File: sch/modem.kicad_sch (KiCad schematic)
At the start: 0 parts

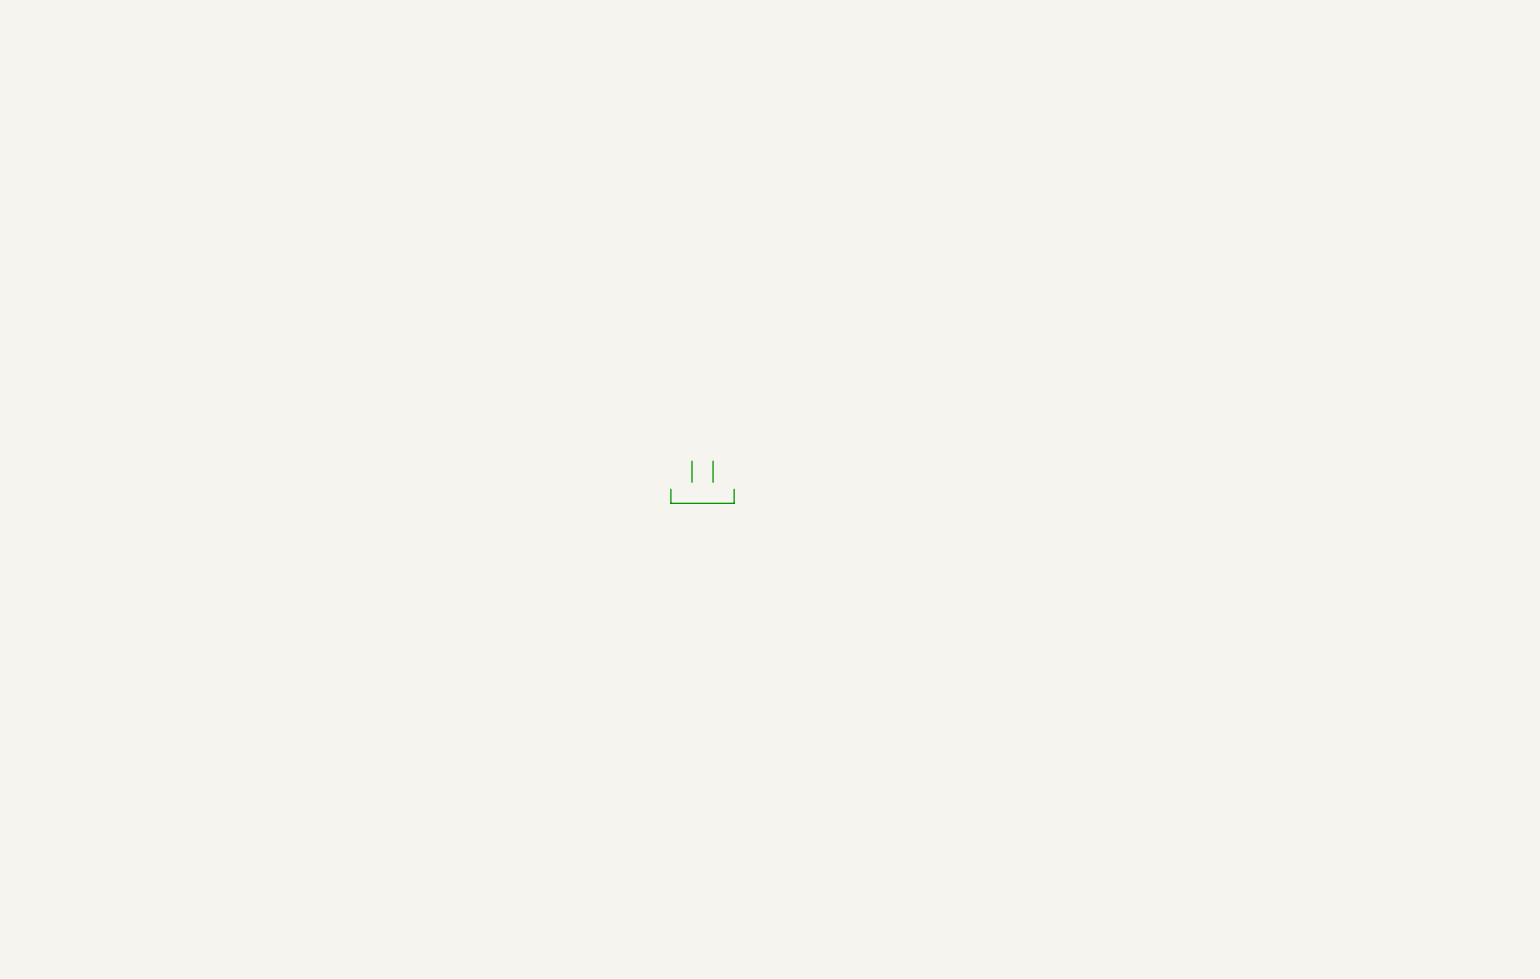
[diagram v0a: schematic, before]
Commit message: Put in Rc7620, not complete
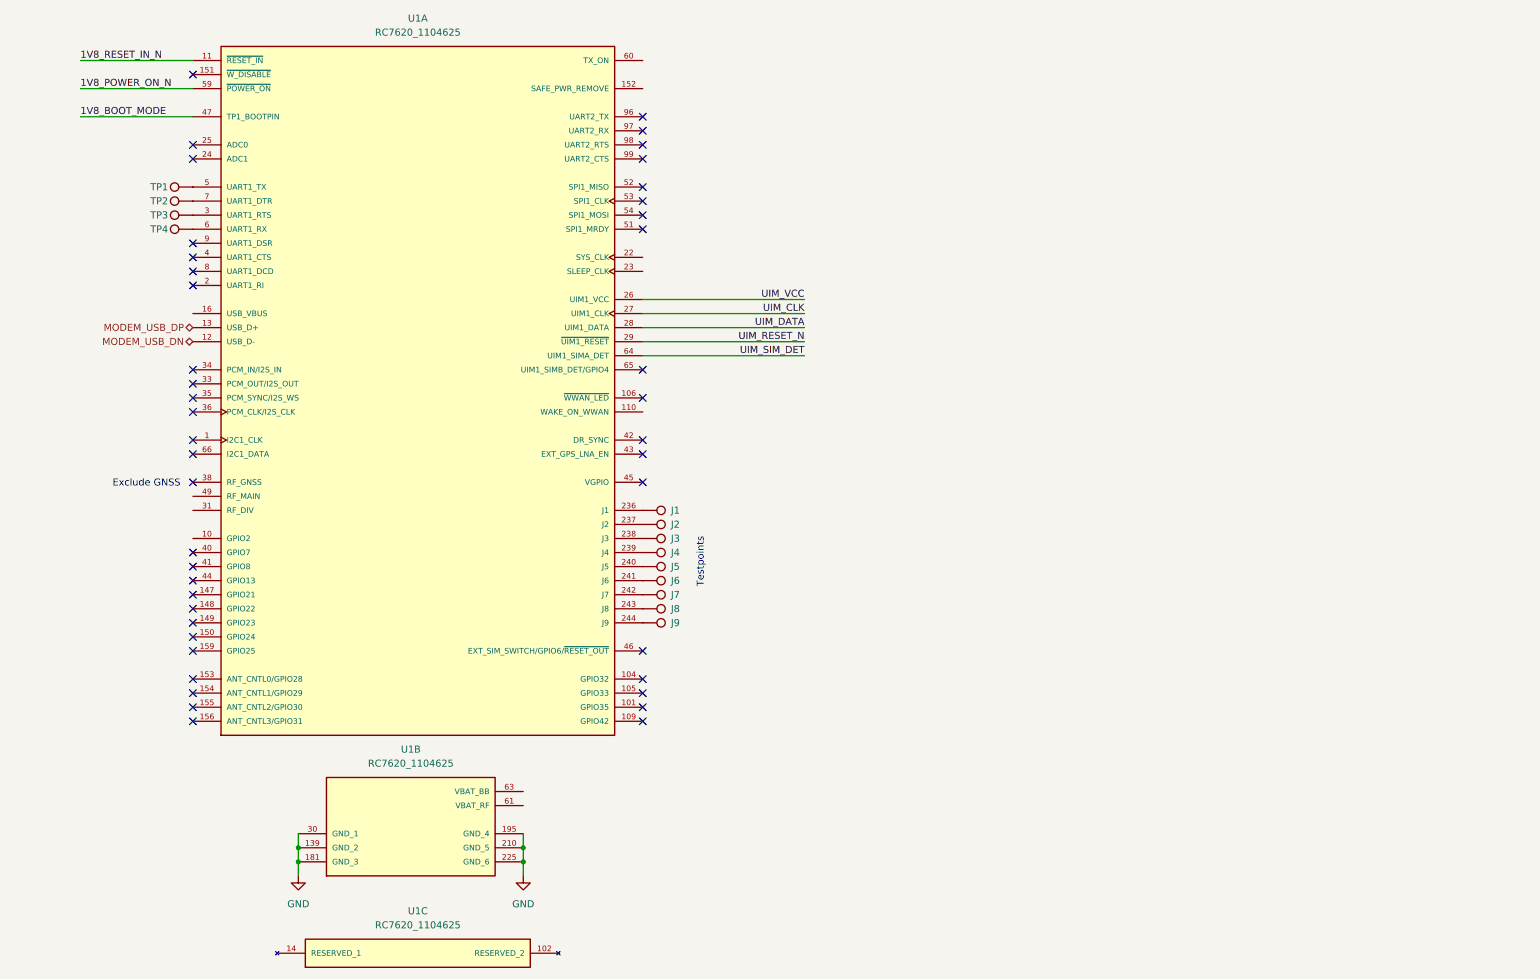
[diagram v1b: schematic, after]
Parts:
- added J1, J2, J3, J4, J5, J6, J7, J8, J9: TestPoint, symbol Connector:TestPoint
- added TP1, TP2, TP3, TP4: T1, symbol Connector:TestPoint
- added U1: RC7620_1104625, RC7620_1104625:XCVR_RC7620_1104625, symbol RC7620_1104625:RC7620_1104625
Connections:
- new net: TP2.1, U1.7 (UART1_DTR)
- new net: TP3.1, U1.3 (UART1_RTS)
- new net: J8.1, U1.243 (J8)
- new net: J7.1, U1.242 (J7)
- new net: J1.1, U1.236 (J1)
- new net: J2.1, U1.237 (J2)
- new net: J3.1, U1.238 (J3)
- new net: J4.1, U1.239 (J4)
- new net: J5.1, U1.240 (J5)
- new net: J6.1, U1.241 (J6)
- new net: J9.1, U1.244 (J9)
- new net: TP1.1, U1.5 (UART1_TX)
- new net: TP4.1, U1.6 (UART1_RX)
- new net: U1.100 (RESERVED_1), U1.14 (RESERVED_1), U1.15 (RESERVED_1), U1.17 (RESERVED_1), U1.18 (RESERVED_1), U1.19 (RESERVED_1), U1.20 (RESERVED_1), U1.21 (RESERVED_1), U1.55 (RESERVED_1), U1.56 (RESERVED_1), U1.57 (RESERVED_1), U1.58 (RESERVED_1), U1.71 (RESERVED_1), U1.72 (RESERVED_1), U1.73 (RESERVED_1), U1.74 (RESERVED_1), U1.75 (RESERVED_1), U1.76 (RESERVED_1), U1.77 (RESERVED_1), U1.78 (RESERVED_1), U1.79 (RESERVED_1), U1.80 (RESERVED_1), U1.81 (RESERVED_1), U1.82 (RESERVED_1), U1.83 (RESERVED_1), U1.84 (RESERVED_1), U1.85 (RESERVED_1), U1.86 (RESERVED_1), U1.87 (RESERVED_1), U1.88 (RESERVED_1), U1.89 (RESERVED_1), U1.90 (RESERVED_1), U1.91 (RESERVED_1), U1.92 (RESERVED_1), U1.93 (RESERVED_1), U1.94 (RESERVED_1), U1.95 (RESERVED_1)
- new net: U1.102 (RESERVED_2), U1.103 (RESERVED_2), U1.107 (RESERVED_2), U1.108 (RESERVED_2), U1.114 (RESERVED_2), U1.115 (RESERVED_2), U1.116 (RESERVED_2), U1.117 (RESERVED_2), U1.118 (RESERVED_2), U1.119 (RESERVED_2), U1.120 (RESERVED_2), U1.121 (RESERVED_2), U1.122 (RESERVED_2), U1.123 (RESERVED_2), U1.124 (RESERVED_2), U1.129 (RESERVED_2), U1.130 (RESERVED_2), U1.131 (RESERVED_2), U1.132 (RESERVED_2), U1.133 (RESERVED_2), U1.134 (RESERVED_2), U1.135 (RESERVED_2), U1.140 (RESERVED_2), U1.141 (RESERVED_2), U1.142 (RESERVED_2), U1.143 (RESERVED_2), U1.144 (RESERVED_2), U1.145 (RESERVED_2), U1.146 (RESERVED_2), U1.160 (RESERVED_2), U1.161 (RESERVED_2), U1.162 (RESERVED_2), U1.163 (RESERVED_2), U1.164 (RESERVED_2), U1.165 (RESERVED_2), U1.166 (RESERVED_2)
- new net 1V8_BOOT_MODE: U1.47 (TP1_BOOTPIN)
- new net 1V8_POWER_ON_N: U1.59 (~{POWER_ON})
- new net 1V8_RESET_IN_N: U1.11 (~{RESET_IN})
- new net GND: U1.111 (GND_1), U1.113 (GND_1), U1.125 (GND_1), U1.128 (GND_1), U1.136 (GND_1), U1.139 (GND_2), U1.167 (GND_2), U1.168 (GND_2), U1.169 (GND_2), U1.170 (GND_2), U1.171 (GND_2), U1.172 (GND_2), U1.173 (GND_2), U1.174 (GND_2), U1.175 (GND_2), U1.176 (GND_2), U1.177 (GND_2), U1.178 (GND_2), U1.179 (GND_2), U1.180 (GND_2), U1.181 (GND_3), U1.182 (GND_3), U1.183 (GND_3), U1.184 (GND_3), U1.185 (GND_3), U1.186 (GND_3), U1.187 (GND_3), U1.188 (GND_3), U1.189 (GND_3), U1.190 (GND_3), U1.191 (GND_3), U1.192 (GND_3), U1.193 (GND_3), U1.194 (GND_3), U1.195 (GND_4), U1.196 (GND_4), U1.197 (GND_4), U1.198 (GND_4), U1.199 (GND_4), U1.200 (GND_4), U1.201 (GND_4), U1.202 (GND_4), U1.203 (GND_4), U1.204 (GND_4), U1.205 (GND_4), U1.206 (GND_4), U1.207 (GND_4), U1.208 (GND_4), U1.209 (GND_4), U1.210 (GND_5), U1.211 (GND_5), U1.212 (GND_5), U1.213 (GND_5), U1.214 (GND_5), U1.215 (GND_5), U1.216 (GND_5), U1.217 (GND_5), U1.218 (GND_5), U1.219 (GND_5), U1.220 (GND_5), U1.221 (GND_5), U1.222 (GND_5), U1.223 (GND_5), U1.224 (GND_5), U1.225 (GND_6), U1.226 (GND_6), U1.227 (GND_6), U1.228 (GND_6), U1.229 (GND_6), U1.230 (GND_6), U1.231 (GND_6), U1.232 (GND_6), U1.233 (GND_6), U1.234 (GND_6), U1.30 (GND_1), U1.32 (GND_1), U1.37 (GND_1), U1.39 (GND_1), U1.48 (GND_1), U1.50 (GND_1), U1.67 (GND_1), U1.68 (GND_1), U1.69 (GND_1), U1.70 (GND_1)
- new net MODEM_USB_DN: U1.12 (USB_D-)
- new net MODEM_USB_DP: U1.13 (USB_D+)
- new net UIM_CLK: U1.27 (UIM1_CLK)
- new net UIM_DATA: U1.28 (UIM1_DATA)
- new net UIM_RESET_N: U1.29 (~{UIM1_RESET})
- new net UIM_SIM_DET: U1.64 (UIM1_SIMA_DET)
- new net UIM_VCC: U1.26 (UIM1_VCC)
- new net VBAT_BB: U1.158 (VBAT_BB), U1.63 (VBAT_BB)
- new net VBAT_RF: U1.157 (VBAT_RF), U1.61 (VBAT_RF), U1.62 (VBAT_RF)
- no-connect marks 0 -> 44
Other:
- note added: "Exclude GNSS"
- note added: "Testpoints"

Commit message: Added powersupply and simcard, still missing 4 ESD diodes to simcard
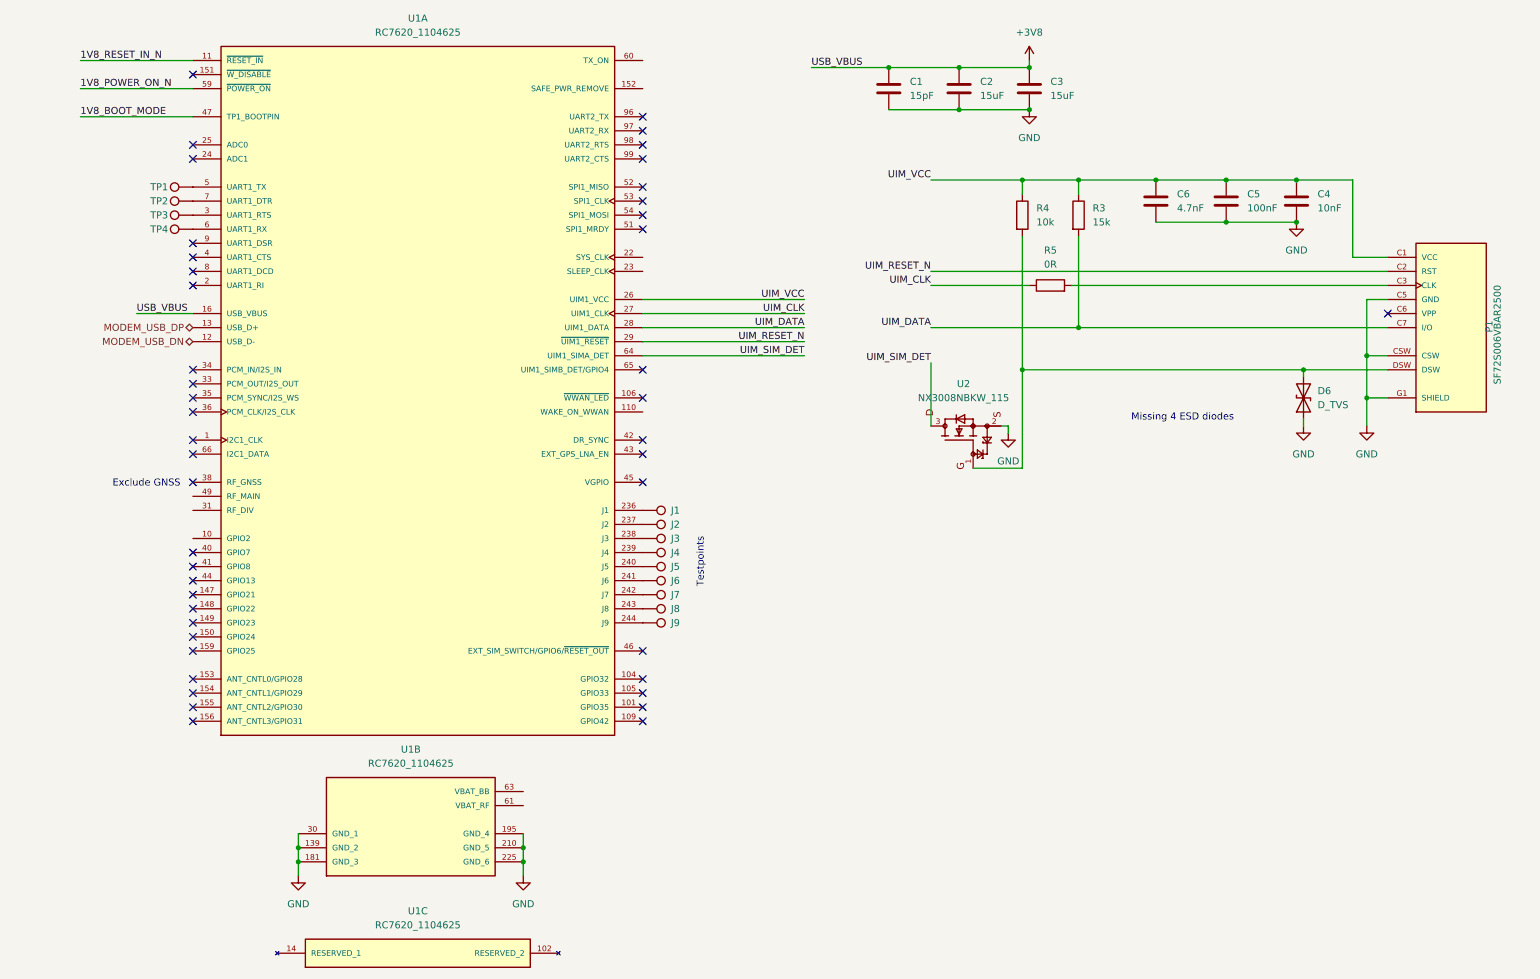
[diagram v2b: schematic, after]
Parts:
- added C1: 15pF, symbol Device:C
- added C2, C3: 15uF, symbol Device:C
- added C4: 10nF, symbol Device:C
- added C5: 100nF, symbol Device:C
- added C6: 4.7nF, symbol Device:C
- added D6: D_TVS, symbol Device:D_TVS
- added P1: SF72S006VBAR2500, SF72S006VBAR2500:JAE_SF72S006VBAR2500, symbol SF72S006VBAR2500:SF72S006VBAR2500
- added R3: 15k, symbol Device:R
- added R4: 10k, symbol Device:R
- added R5: 0R, symbol Device:R
- added U2: NX3008NBKW_115, NX3008NBKW_115:SOT65P210X110-3N, symbol NX3008NBKW_115:NX3008NBKW_115
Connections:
- net GND: now also C1.2, C2.2, C3.2, C4.2, C5.2, C6.2, D6.1 (A1), P1.C5 (GND), P1.CSW, P1.G1 (SHIELD), P1.G10 (SHIELD), P1.G2 (SHIELD), P1.G3 (SHIELD), P1.G4 (SHIELD), P1.G5 (SHIELD), P1.G6 (SHIELD), P1.G7 (SHIELD), P1.G8 (SHIELD), P1.G9 (SHIELD), U2.2
- net UIM_CLK: now also R5.1
- net UIM_DATA: now also P1.C7 (I/O), R3.2
- net UIM_RESET_N: now also P1.C2 (RST)
- net UIM_SIM_DET: now also U2.3
- net UIM_VCC: now also C4.1, C5.1, C6.1, P1.C1 (VCC), R3.1, R4.1
- net +3V8: now reaches U1.16 (USB_VBUS)
- net +3V8: now also C1.1, C2.1, C3.1
- new net: P1.C3 (CLK), R5.2
- new net: D6.2 (A2), P1.DSW, R4.2, U2.1
- no-connect marks 44 -> 45
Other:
- note added: "Missing 4 ESD diodes"

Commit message: All pins connected the same way as in BUGG, no footprints added
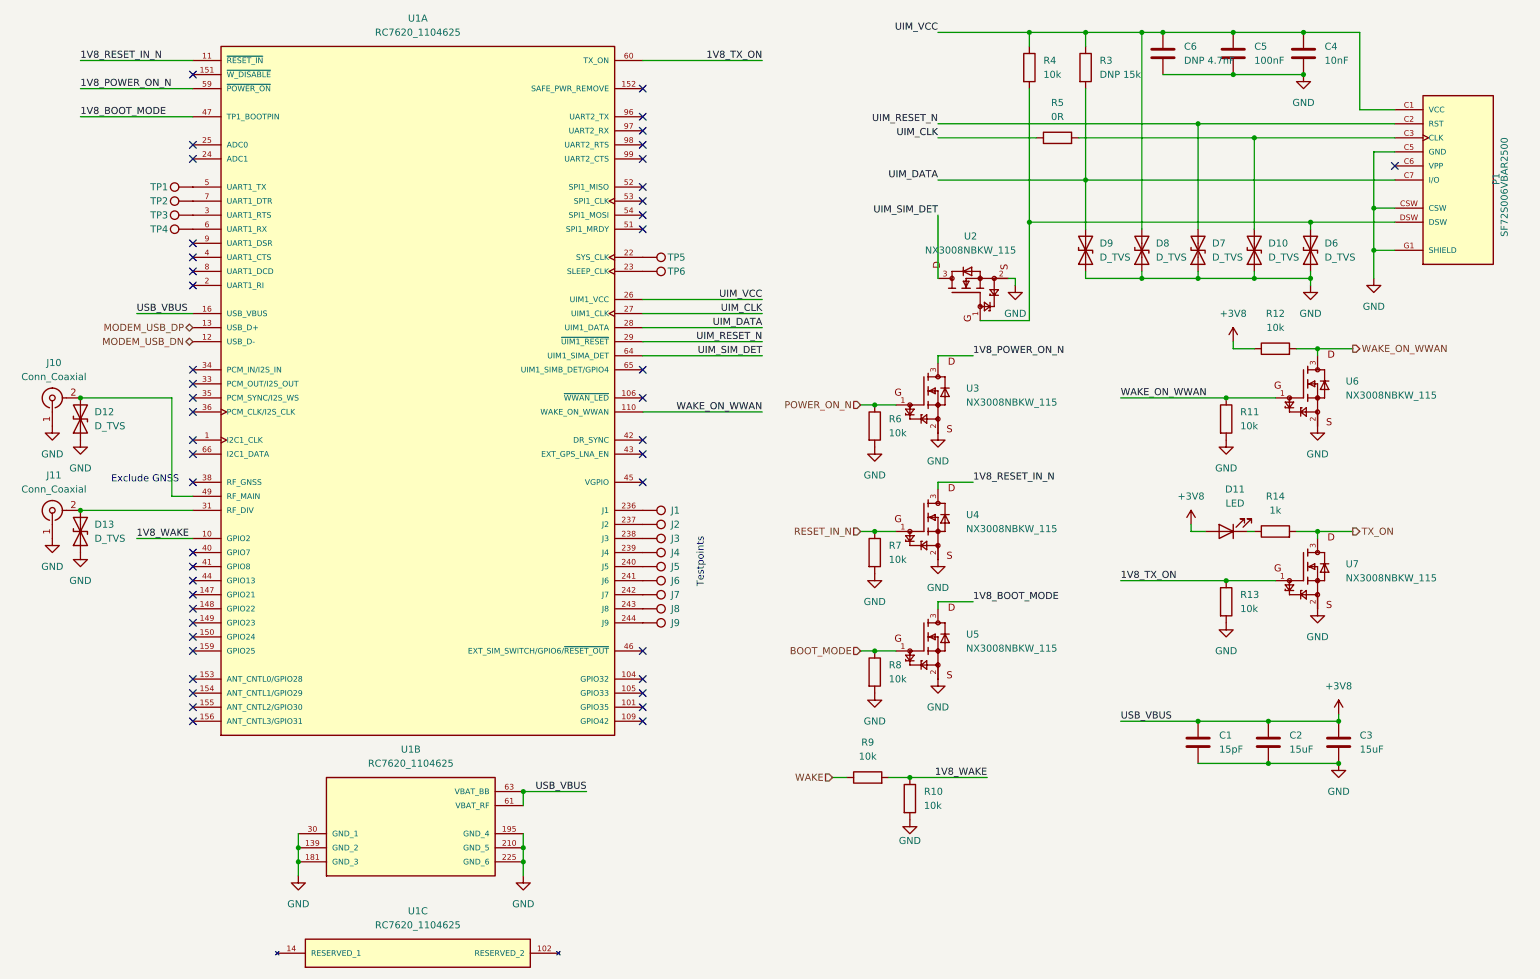
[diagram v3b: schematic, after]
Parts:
- added D10, D12, D13, D7, D8, D9: D_TVS, symbol Device:D_TVS
- added D11: LED, symbol Device:LED
- added J10, J11: Conn_Coaxial, symbol Connector:Conn_Coaxial
- added R10, R11, R12, R13, R6, R7, R8, R9: 10k, symbol Device:R
- added R14: 1k, symbol Device:R
- added TP5, TP6: T1, symbol Connector:TestPoint
- added U3, U4, U5, U6, U7: NX3008NBKW_115, NX3008NBKW_115:SOT65P210X110-3N, symbol NX3008NBKW_115:NX3008NBKW_115
- C6: value 4.7nF -> DNP 4.7nF
- R3: value 15k -> DNP 15k
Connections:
- net VBAT_BB is gone; now on net +3V8: U1.158 (VBAT_BB), U1.63 (VBAT_BB)
- net VBAT_RF is gone; now on net +3V8: U1.157 (VBAT_RF), U1.61 (VBAT_RF), U1.62 (VBAT_RF)
- net +3V8: now also D11.2 (A), R12.1
- net 1V8_BOOT_MODE: now also U5.3
- net 1V8_POWER_ON_N: now also U3.3
- net 1V8_RESET_IN_N: now also U4.3
- net GND: now also D10.1 (A1), D12.1 (A1), D13.1 (A1), D7.1 (A1), D8.1 (A1), D9.1 (A1), J10.1 (In), J11.1 (In), R10.2, R11.2, R13.2, R6.2, R7.2, R8.2, U3.2, U4.2, U5.2, U6.2, U7.2
- net UIM_DATA: now also D9.2 (A2)
- net UIM_RESET_N: now also D7.2 (A2)
- net UIM_VCC: now also D8.2 (A2)
- net at P1.C3 (CLK), R5.2: now also D10.2 (A2)
- net 1V8_WAKE: now reaches U1.10 (GPIO2)
- net 1V8_WAKE: now also R10.1, R9.2
- net WAKE_ON_WWAN: now reaches U1.110 (WAKE_ON_WWAN)
- net WAKE_ON_WWAN: now also R11.1, R12.2, U6.1, U6.3
- net at U1.22 (SYS_CLK): now also TP5.1
- net at U1.23 (SLEEP_CLK): now also TP6.1
- net at U1.31 (RF_DIV): now also D13.2 (A2), J11.2 (Ext)
- net at U1.49 (RF_MAIN): now also D12.2 (A2), J10.2 (Ext)
- net 1V8_TX_ON: now reaches U1.60 (TX_ON)
- net 1V8_TX_ON: now also R13.1, U7.1
- new net: D11.1 (K), R14.1
- new net BOOT_MODE: R8.1, U5.1
- new net POWER_ON_N: R6.1, U3.1
- new net RESET_IN_N: R7.1, U4.1
- new net TX_ON: R14.2, U7.3
- new net WAKE: R9.1
- no-connect marks 45 -> 46
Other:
- note removed: "Missing 4 ESD diodes"
- moved on the sheet: C1, C2, C3, C4, C5, C6, D6, P1, R3, R4, R5, U2

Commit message: added cap footprints and part numbers
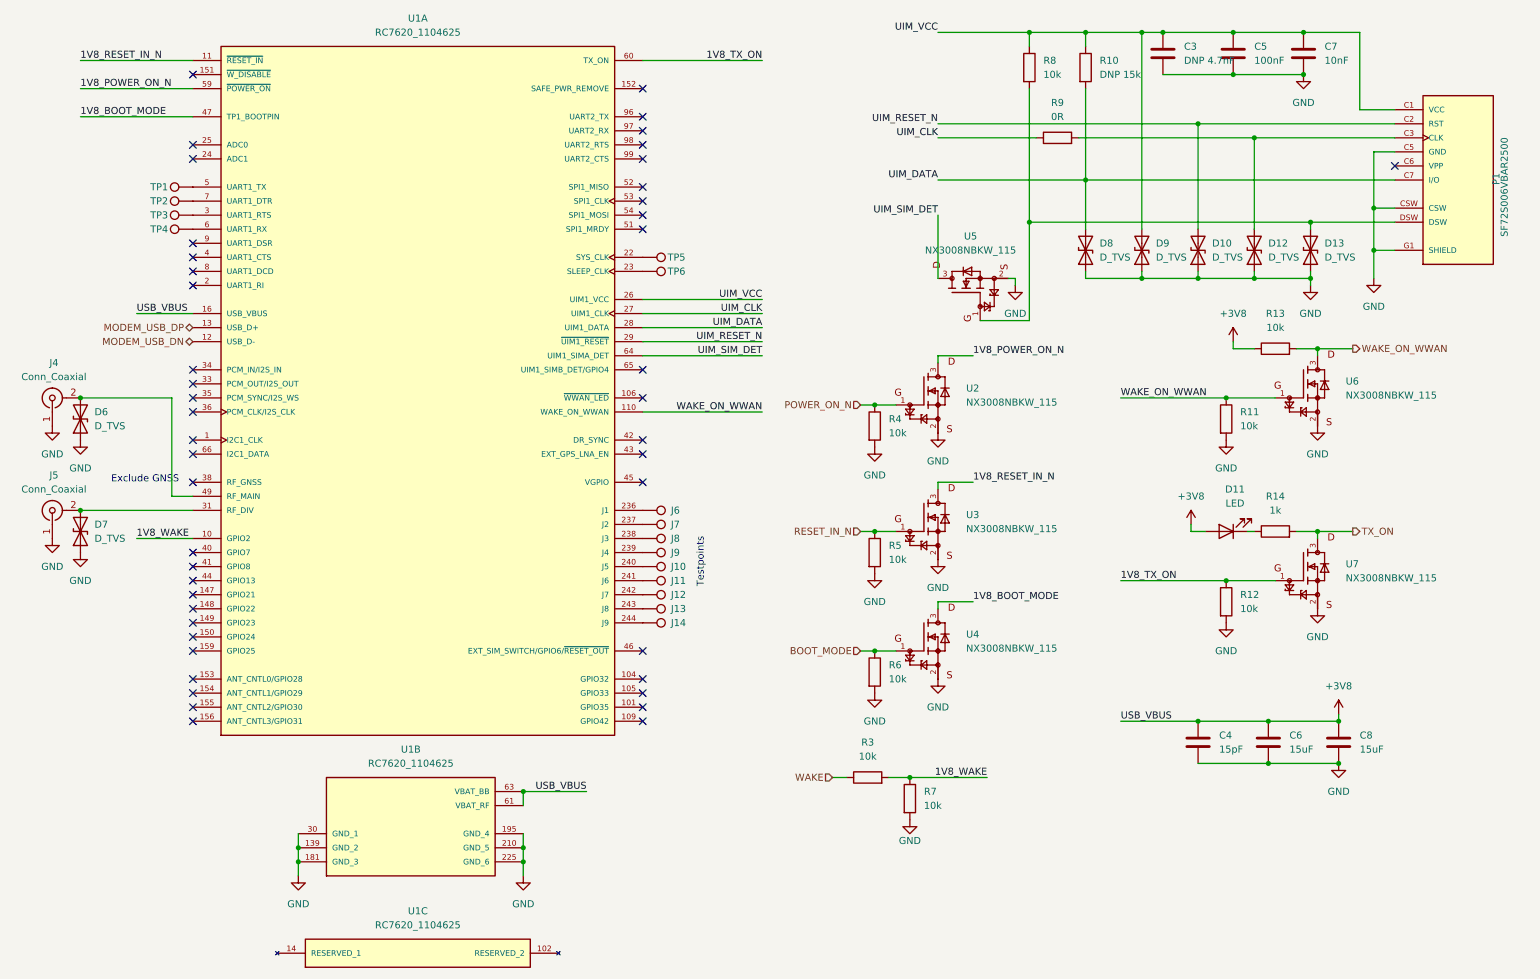
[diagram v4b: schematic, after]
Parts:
- C4: renamed from C1; footprint (none) -> Capacitor_SMD:C_0603_1608Metric; MPN (none) -> C1608X5R0J156M080AC
- C5: footprint (none) -> Capacitor_SMD:C_0603_1608Metric; MPN (none) -> C0603C104K3RACTU
- C6: renamed from C2; footprint (none) -> Capacitor_SMD:C_0603_1608Metric; MPN (none) -> C1608X5R0J156M080AC
- C7: renamed from C4; footprint (none) -> Capacitor_SMD:C_0603_1608Metric; MPN (none) -> C0603C103K5RACTU
- C8: renamed from C3; footprint (none) -> Capacitor_SMD:C_0603_1608Metric; MPN (none) -> C1608X5R0J156M080AC
- renumbered C6 to C3, D7 to D10, D10 to D12, D6 to D13, D12 to D6, D13 to D7, D9 to D8, D8 to D9, J5 to J10, J6 to J11, J7 to J12, J8 to J13, J9 to J14, J10 to J4, J11 to J5, J1 to J6, J2 to J7, J3 to J8, J4 to J9, R3 to R10, R13 to R12, R12 to R13, R9 to R3, R6 to R4, R7 to R5, R8 to R6, R10 to R7, R4 to R8, R5 to R9, U3 to U2, U4 to U3, U5 to U4, U2 to U5
